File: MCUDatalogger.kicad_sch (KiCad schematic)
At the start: 1 part

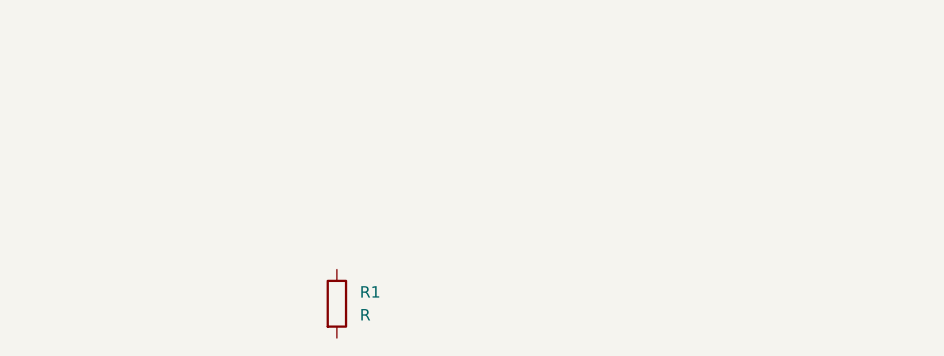
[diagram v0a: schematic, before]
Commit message: Added a resistor.
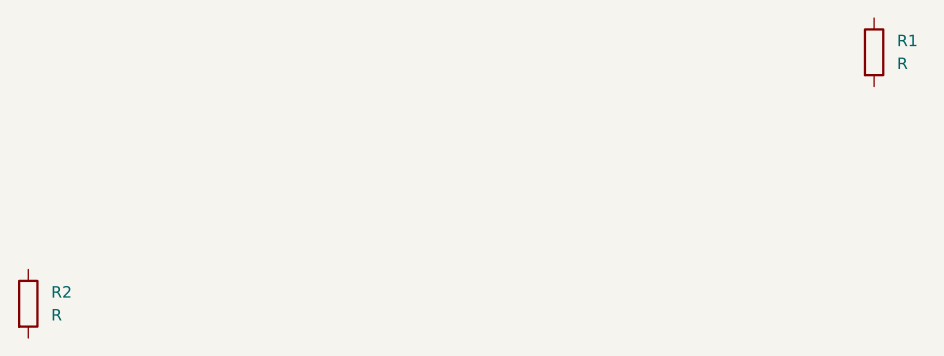
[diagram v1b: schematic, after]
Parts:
- added R2: R, symbol Device:R
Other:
- moved on the sheet: R1
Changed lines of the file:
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@@
 (kicad_sch (version 20230121) (generator eeschema)
   (paper "A4")
-  (symbol (lib_id "Device:R") (at 124.46 72.39 0) (unit 1)
+  (symbol (lib_id "Device:R") (at 90.17 72.39 0) (unit 1)
     (in_bom yes) (on_board yes) (dnp no) (fields_autoplaced)
-    (property "Reference" "R1" (at 127 71.12 0)
+    (property "Reference" "R2" (at 92.71 71.12 0)
       (effects (font (size 1.27 1.27)) (justify left))
     )
-    (property "Value" "R" (at 127 73.66 0)
+    (property "Value" "R" (at 92.71 73.66 0)
       (effects (font (size 1.27 1.27)) (justify left))
     )
-    (property "Footprint" "" (at 122.682 72.39 90)
+    (property "Footprint" "" (at 88.392 72.39 90)
       (effects (font (size 1.27 1.27)) hide)
     )
-    (property "Datasheet" "~" (at 124.46 72.39 0)
+    (property "Datasheet" "~" (at 90.17 72.39 0)
       (effects (font (size 1.27 1.27)) hide)
     )
+    (pin "2")
+    (pin "1")
+    (instances
+      (project "MCUDatalogger"
+        (path "/a46afdbf-01b2-4464-8083-80e47ae67da1"
+          (reference "R2") (unit 1)
+        )
+      )
+    )
+  )
+  (symbol (lib_id "Device:R") (at 184.15 44.45 0) (unit 1)
+    (in_bom yes) (on_board yes) (dnp no) (fields_autoplaced)
+    (property "Reference" "R1" (at 186.69 43.18 0)
+      (effects (font (size 1.27 1.27)) (justify left))
+    )
+    (property "Value" "R" (at 186.69 45.72 0)
+      (effects (font (size 1.27 1.27)) (justify left))
+    )
+    (property "Footprint" "" (at 182.372 44.45 90)
+      (effects (font (size 1.27 1.27)) hide)
+    )
+    (property "Datasheet" "~" (at 184.15 44.45 0)
+      (effects (font (size 1.27 1.27)) hide)
+    )

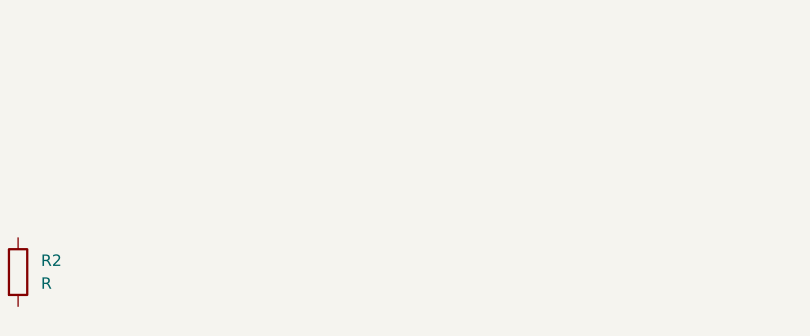
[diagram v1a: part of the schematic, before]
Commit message: Added capacitor.
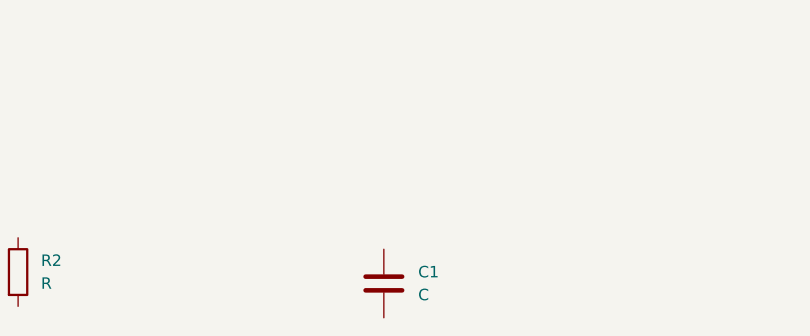
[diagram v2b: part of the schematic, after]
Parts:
- added C1: C, symbol Device:C
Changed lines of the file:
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@@
 (kicad_sch (version 20230121) (generator eeschema)
   (paper "A4")
+  (symbol (lib_id "Device:C") (at 130.81 73.66 0) (unit 1)
+    (in_bom yes) (on_board yes) (dnp no) (fields_autoplaced)
+    (property "Reference" "C1" (at 134.62 72.39 0)
+      (effects (font (size 1.27 1.27)) (justify left))
+    )
+    (property "Value" "C" (at 134.62 74.93 0)
+      (effects (font (size 1.27 1.27)) (justify left))
+    )
+    (property "Footprint" "" (at 131.7752 77.47 0)
+      (effects (font (size 1.27 1.27)) hide)
+    )
+    (property "Datasheet" "~" (at 130.81 73.66 0)
+      (effects (font (size 1.27 1.27)) hide)
+    )
+    (pin "2")
+    (pin "1")
+    (instances
+      (project "MCUDatalogger"
+        (path "/a46afdbf-01b2-4464-8083-80e47ae67da1"
+          (reference "C1") (unit 1)
+        )
+      )
+    )
+  )
   (symbol (lib_id "Device:R") (at 90.17 72.39 0) (unit 1)
     (in_bom yes) (on_board yes) (dnp no) (fields_autoplaced)

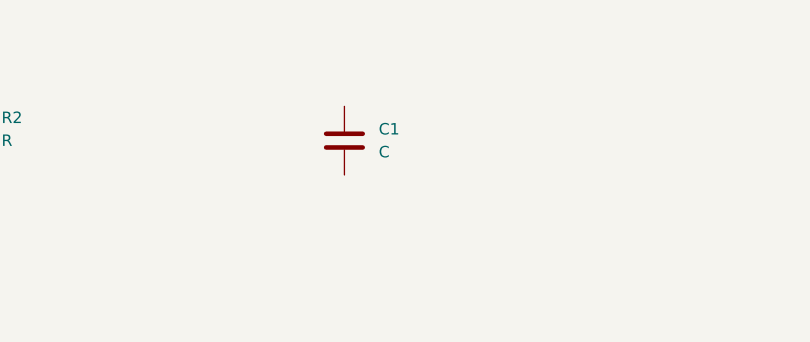
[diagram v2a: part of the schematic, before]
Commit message: Another resistor and capacitor added
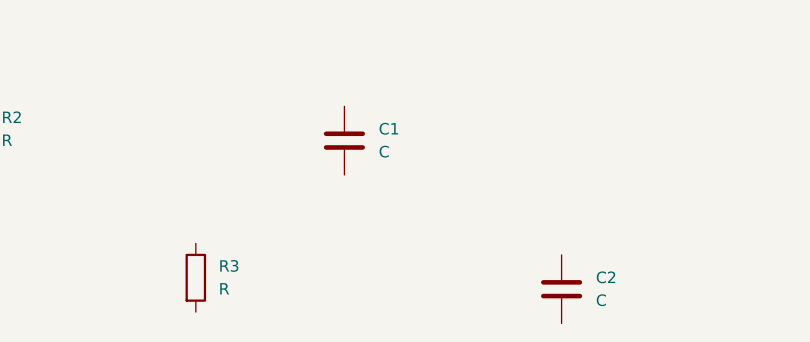
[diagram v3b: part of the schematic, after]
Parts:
- added C2: C, symbol Device:C
- added R3: R, symbol Device:R
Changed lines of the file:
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@@
 (kicad_sch (version 20230121) (generator eeschema)
   (paper "A4")
+  (symbol (lib_id "Device:R") (at 114.3 88.9 0) (unit 1)
+    (in_bom yes) (on_board yes) (dnp no) (fields_autoplaced)
+    (property "Reference" "R3" (at 116.84 87.63 0)
+      (effects (font (size 1.27 1.27)) (justify left))
+    )
+    (property "Value" "R" (at 116.84 90.17 0)
+      (effects (font (size 1.27 1.27)) (justify left))
+    )
+    (property "Footprint" "" (at 112.522 88.9 90)
+      (effects (font (size 1.27 1.27)) hide)
+    )
+    (property "Datasheet" "~" (at 114.3 88.9 0)
+      (effects (font (size 1.27 1.27)) hide)
+    )
+    (pin "2")
+    (pin "1")
+    (instances
+      (project "MCUDatalogger"
+        (path "/a46afdbf-01b2-4464-8083-80e47ae67da1"
+          (reference "R3") (unit 1)
+        )
+      )
+    )
+  )
+  (symbol (lib_id "Device:C") (at 154.94 90.17 0) (unit 1)
+    (in_bom yes) (on_board yes) (dnp no) (fields_autoplaced)
+    (property "Reference" "C2" (at 158.75 88.9 0)
+      (effects (font (size 1.27 1.27)) (justify left))
+    )
+    (property "Value" "C" (at 158.75 91.44 0)
+      (effects (font (size 1.27 1.27)) (justify left))
+    )
+    (property "Footprint" "" (at 155.9052 93.98 0)
+      (effects (font (size 1.27 1.27)) hide)
+    )
+    (property "Datasheet" "~" (at 154.94 90.17 0)
+      (effects (font (size 1.27 1.27)) hide)
+    )
+    (pin "2")
+    (pin "1")
+    (instances
+      (project "MCUDatalogger"
+        (path "/a46afdbf-01b2-4464-8083-80e47ae67da1"
+          (reference "C2") (unit 1)
+        )
+      )
+    )
+  )
   (symbol (lib_id "Device:C") (at 130.81 73.66 0) (unit 1)
     (in_bom yes) (on_board yes) (dnp no) (fields_autoplaced)

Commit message: Added some text
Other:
- note added: "This is just a test"
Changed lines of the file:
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@@
 (kicad_sch (version 20230121) (generator eeschema)
   (paper "A4")
+  (text "This is just a test" (at 128.27 57.15 0)
+    (effects (font (size 1.27 1.27)) (justify left bottom))
+  )
   (symbol (lib_id "Device:R") (at 114.3 88.9 0) (unit 1)
     (in_bom yes) (on_board yes) (dnp no) (fields_autoplaced)

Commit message: Update MCUDatalogger.kicad_sch
just a test
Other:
- note added: "This is just a test for pulling request"
- note removed: "This is just a test"
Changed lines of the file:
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@@
 (kicad_sch (version 20230121) (generator eeschema)
   (paper "A4")
-  (text "This is just a test" (at 128.27 57.15 0)
+  (text "This is just a test for pulling request" (at 128.27 57.15 0)
     (effects (font (size 1.27 1.27)) (justify left bottom))
   )

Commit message: Setup of EESchema for new project
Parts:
- removed C1, C2: C, symbol Device:C
- removed R1, R2, R3: R, symbol Device:R
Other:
- note removed: "This is just a test for pulling request"
- title: (none) -> ${project_name}
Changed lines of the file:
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@@
 (kicad_sch (version 20230121) (generator eeschema)
   (paper "A4")
-  (text "This is just a test for pulling request" (at 128.27 57.15 0)
-    (effects (font (size 1.27 1.27)) (justify left bottom))
-  )
-  (symbol (lib_id "Device:R") (at 114.3 88.9 0) (unit 1)
-    (in_bom yes) (on_board yes) (dnp no) (fields_autoplaced)
-    (property "Reference" "R3" (at 116.84 87.63 0)
-      (effects (font (size 1.27 1.27)) (justify left))
-    )
-    (property "Value" "R" (at 116.84 90.17 0)
-      (effects (font (size 1.27 1.27)) (justify left))
-    )
-    (property "Footprint" "" (at 112.522 88.9 90)
-      (effects (font (size 1.27 1.27)) hide)
-    )
-    (property "Datasheet" "~" (at 114.3 88.9 0)
-      (effects (font (size 1.27 1.27)) hide)
-    )
-    (pin "2")
-    (pin "1")
-    (instances
-      (project "MCUDatalogger"
-        (path "/a46afdbf-01b2-4464-8083-80e47ae67da1"
-          (reference "R3") (unit 1)
-        )
-      )
-    )
-  )
-  (symbol (lib_id "Device:C") (at 154.94 90.17 0) (unit 1)
-    (in_bom yes) (on_board yes) (dnp no) (fields_autoplaced)
-    (property "Reference" "C2" (at 158.75 88.9 0)
-      (effects (font (size 1.27 1.27)) (justify left))
-    )
-    (property "Value" "C" (at 158.75 91.44 0)
-      (effects (font (size 1.27 1.27)) (justify left))
-    )
-    (property "Footprint" "" (at 155.9052 93.98 0)
-      (effects (font (size 1.27 1.27)) hide)
-    )
-    (property "Datasheet" "~" (at 154.94 90.17 0)
-      (effects (font (size 1.27 1.27)) hide)
-    )
-    (pin "2")
-    (pin "1")
-    (instances
-      (project "MCUDatalogger"
-        (path "/a46afdbf-01b2-4464-8083-80e47ae67da1"
-          (reference "C2") (unit 1)
-        )
-      )
-    )
-  )
-  (symbol (lib_id "Device:C") (at 130.81 73.66 0) (unit 1)
-    (in_bom yes) (on_board yes) (dnp no) (fields_autoplaced)
-    (property "Reference" "C1" (at 134.62 72.39 0)
-      (effects (font (size 1.27 1.27)) (justify left))
-    )
-    (property "Value" "C" (at 134.62 74.93 0)
-      (effects (font (size 1.27 1.27)) (justify left))
-    )
-    (property "Footprint" "" (at 131.7752 77.47 0)
-      (effects (font (size 1.27 1.27)) hide)
-    )
-    (property "Datasheet" "~" (at 130.81 73.66 0)
-      (effects (font (size 1.27 1.27)) hide)
-    )
-    (pin "2")
-    (pin "1")
-    (instances
-      (project "MCUDatalogger"
-        (path "/a46afdbf-01b2-4464-8083-80e47ae67da1"
-          (reference "C1") (unit 1)
-        )
-      )
-    )
-  )
-  (symbol (lib_id "Device:R") (at 90.17 72.39 0) (unit 1)
-    (in_bom yes) (on_board yes) (dnp no) (fields_autoplaced)
-    (property "Reference" "R2" (at 92.71 71.12 0)
-      (effects (font (size 1.27 1.27)) (justify left))
-    )
-    (property "Value" "R" (at 92.71 73.66 0)
-      (effects (font (size 1.27 1.27)) (justify left))
-    )
-    (property "Footprint" "" (at 88.392 72.39 90)
-      (effects (font (size 1.27 1.27)) hide)
-    )
-    (property "Datasheet" "~" (at 90.17 72.39 0)
-      (effects (font (size 1.27 1.27)) hide)
-    )
-    (pin "2")
-    (pin "1")
-    (instances
-      (project "MCUDatalogger"
-        (path "/a46afdbf-01b2-4464-8083-80e47ae67da1"
-          (reference "R2") (unit 1)
-        )
-      )
-    )
-  )
-  (symbol (lib_id "Device:R") (at 184.15 44.45 0) (unit 1)
-    (in_bom yes) (on_board yes) (dnp no) (fields_autoplaced)
-    (property "Reference" "R1" (at 186.69 43.18 0)
-      (effects (font (size 1.27 1.27)) (justify left))
-    )
-    (property "Value" "R" (at 186.69 45.72 0)
-      (effects (font (size 1.27 1.27)) (justify left))
-    )
-    (property "Footprint" "" (at 182.372 44.45 90)
-      (effects (font (size 1.27 1.27)) hide)
-    )
-    (property "Datasheet" "~" (at 184.15 44.45 0)
-      (effects (font (size 1.27 1.27)) hide)
-    )
-    (pin "2")
-    (pin "1")
-    (instances
-      (project "MCUDatalogger"
-        (path "/a46afdbf-01b2-4464-8083-80e47ae67da1"
-          (reference "R1") (unit 1)
-        )
-      )
-    )
+  (title_block
+    (title "${project_name}")
+    (date "2024-10-19")
+    (rev "1")
   )
   (sheet_instances

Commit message: Have added required symbols to the schematic sheets.
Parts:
- added BT1: Battery, symbol Device:Battery
- added C1, C2, C3, C4: C, symbol Device:C
- added C5: C_Polarized, symbol Device:C_Polarized
- added D1, D2: LED, symbol Device:LED
- added H1, H2, H3, H4: MountingHole, symbol Mechanical:MountingHole
- added R1, R2, R3, R4, R5, R6, R7: R, symbol Device:R
- added U1, U2: 24LC1025, symbol Memory_EEPROM:24LC1025
- added U3: DS1337S_, SOIC127P600X175-8N, symbol DS1337S_:DS1337S_
- added U4: ATMEGA328P-AU, QFP80P900X900X120-32N, symbol ATMEGA328P-AU:ATMEGA328P-AU
- added Y1, Y2: Crystal, symbol Device:Crystal
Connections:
- new net: U4.21 (GND), U4.3 (GND), U4.5 (GND)
- new net: U4.4 (VCC), U4.6 (VCC)
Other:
- added sheet Connectors (Connectors.kicad_sch)
